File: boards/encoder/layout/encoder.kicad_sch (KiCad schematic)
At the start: 6 parts, among them IC1 AS5047U-HTSM, J1 EncoderTab

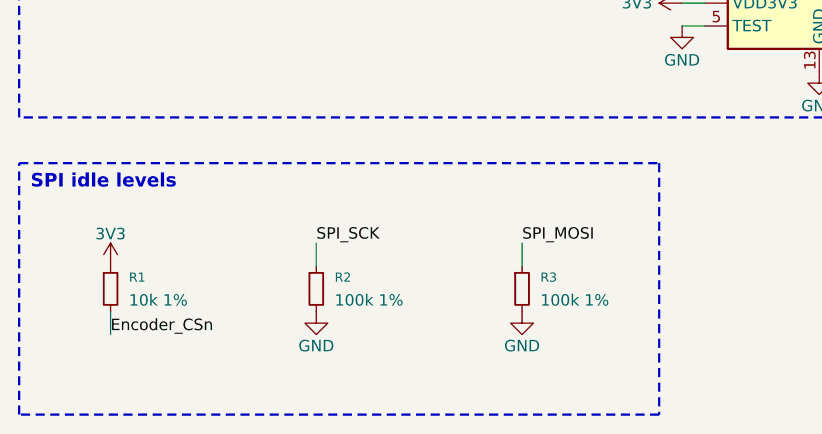
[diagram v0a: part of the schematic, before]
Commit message: ✨ Place the schematics from per-sheet placement files: the tool's fixes, the B02B pin names, docs, and the encoder, Bluetooth and DRIVERS placements for this revision
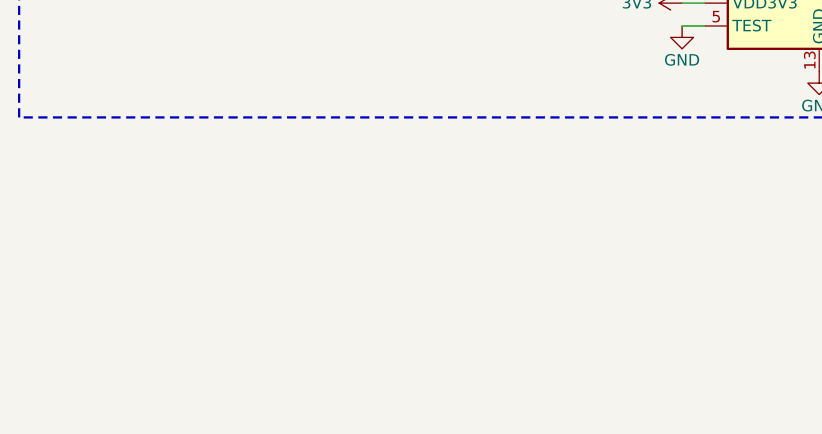
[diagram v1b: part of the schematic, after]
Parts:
- removed R1: 10k 1%, stdlib_kicad-footprints_Resistor_SMD:R_0402_1005Metric, symbol R_Small
- removed R2, R3: 100k 1%, stdlib_kicad-footprints_Resistor_SMD:R_0402_1005Metric, symbol R_Small
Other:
- note removed: "SPI idle levels"
